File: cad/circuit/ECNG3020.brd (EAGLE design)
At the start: 100 x 61 mm, 30 parts, among them Q1 16Mhz, T1 2N3904, T2 2N3904, T3 2N3904, T4 2N3904, T5 2N3904, U1 ATMEGA328P-PU, X1 22-23-2021, X2 22-23-2021, X3 22-23-2021, X4 22-23-2021, X5 22-23-2021, X6 22-23-2021, X7 22-23-2021

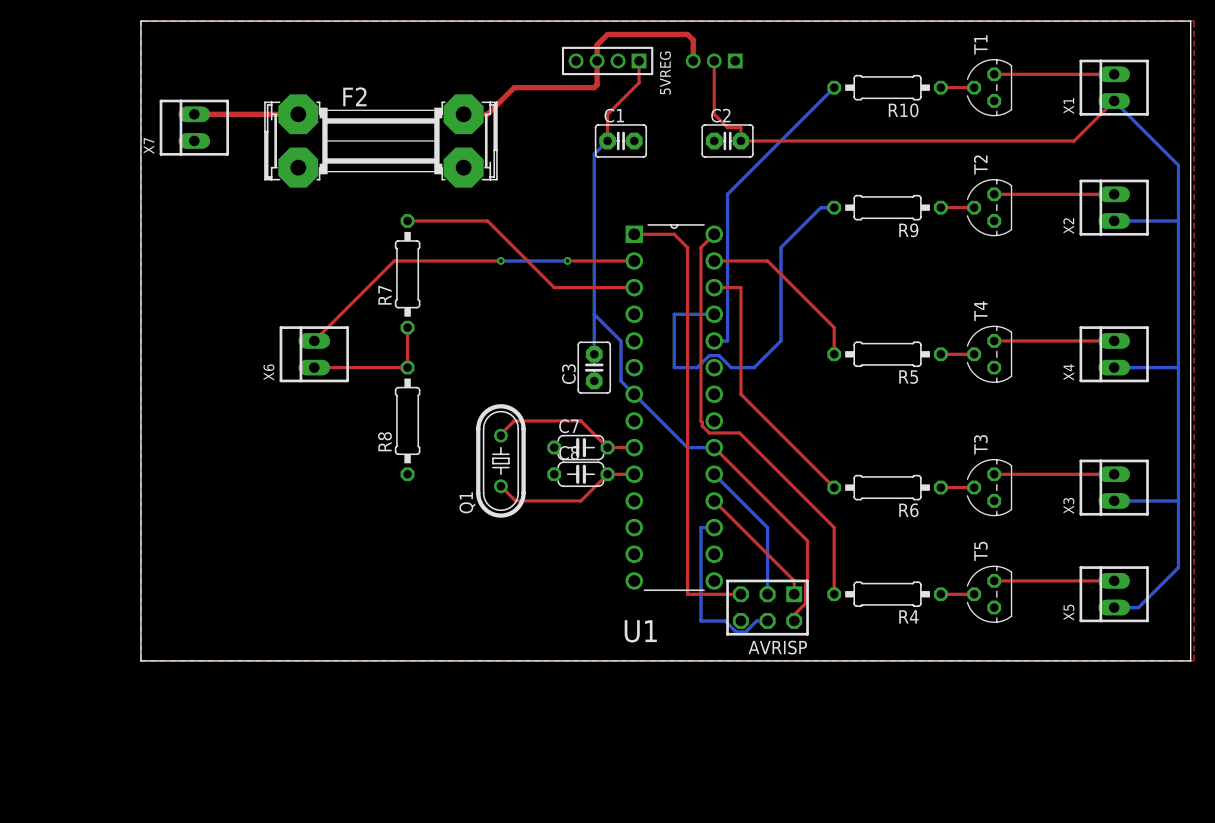
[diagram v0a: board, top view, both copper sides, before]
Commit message: Updated the PCB to use I2C instead of UART
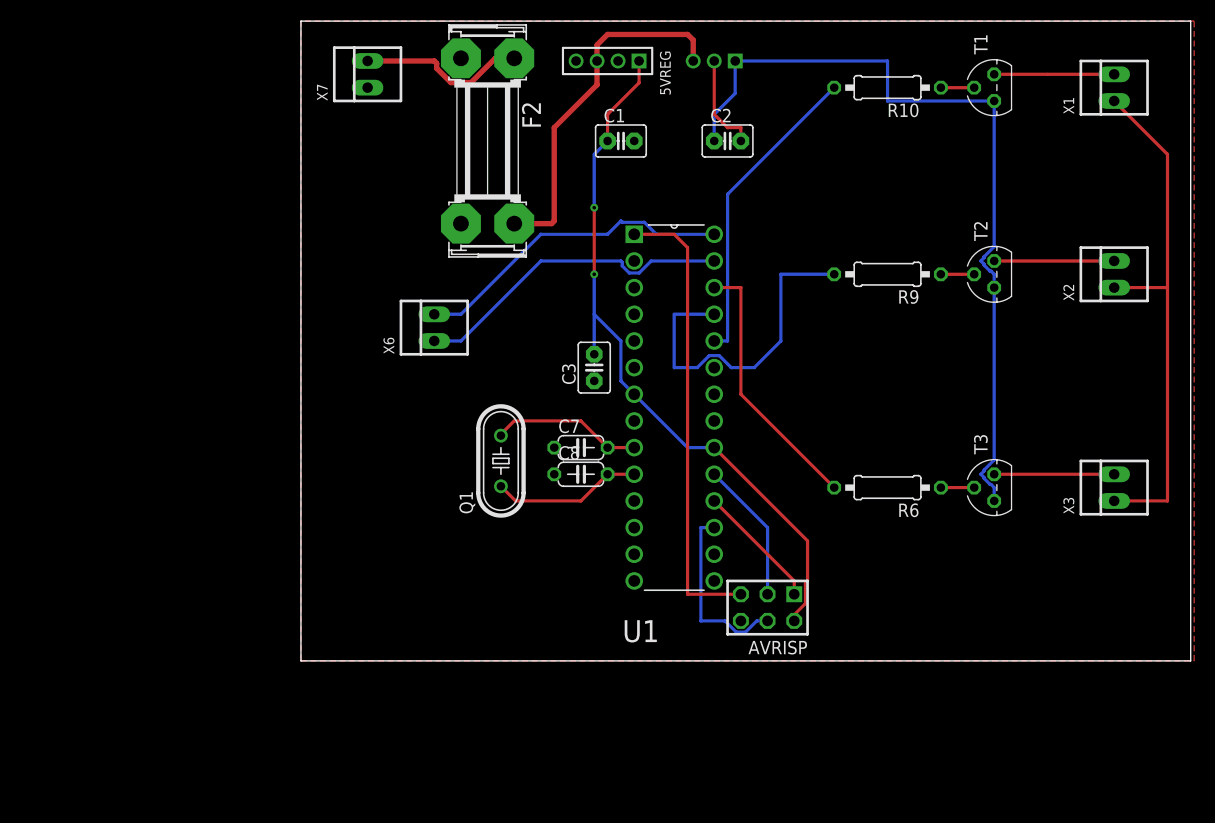
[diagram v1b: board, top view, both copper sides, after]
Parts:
- removed R4, R5, R8: 10k, rcl:0207/10
- removed R7: 5k1, rcl:0207/10
- removed T4, T5: 2N3904, transistor-neu-to92:TO92
- removed X4, X5: 22-23-2021, con-molex:22-23-2021
- moved X7 17.3 mm to (33.0, 68.6)
- moved X6 11.7 mm to (39.4, 44.5)
- moved F2 10.2 mm to (44.5, 62.2), turned to 270 degrees
- moved R9 6.35 mm to (82.5, 49.5)
- moved T2 6.35 mm to (92.7, 49.5)
- moved X2 6.35 mm to (104.1, 49.5)
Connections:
- removed net N$16: R5.1, T4.2
- removed net N$17: R5.2, U1.27
- removed net N$18: R4.2, U1.28
- removed net N$8: T5.1, X5.2
- removed net N$9: T4.1, X4.2
- removed net RX: R7.1, R8.2, X6.1
- new net SCL: U1.28, X6.2
- new net SDA: U1.27, X6.1
- net 3.3: no longer X1.1, X2.1, X3.1, X4.1, X5.1
- net GND: no longer R8.1, T4.3, T5.3
- net N$7: now also X1.1, X2.1, X3.1; no longer R4.1, T5.2
- net RXM: no longer X6.2
- net TXM: no longer R7.2
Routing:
- net 3.3: track 119.6 -> 9.42 mm
- net GND: track 0.00 -> 77.2 mm
- net N$7: track 3.18 -> 50.4 mm
- net N$18: track 41.8 -> 0.00 mm
- net RXM: track 33.6 -> 0.00 mm, vias 2 -> 0
- net SDA: track 0.00 -> 31.0 mm
- net SCL: track 0.00 -> 30.9 mm
- net TXM: track 24.2 -> 0.00 mm
- net N$17: track 16.6 -> 0.00 mm
- net RX: track 12.7 -> 0.00 mm
- net N$9: track 11.4 -> 0.00 mm
- net N$8: track 11.4 -> 0.00 mm
- net N$13: track 9.91 -> 16.1 mm
- net 12V: track 29.5 -> 34.2 mm
- net N$2: track 36.6 -> 32.5 mm
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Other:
- board size 100 x 61 mm -> 84.8 x 61 mm

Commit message: Updated the schematic and board
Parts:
- moved R10 50.7 mm to (63.5, 20.3)
- moved T1 50.2 mm to (74.9, 20.3)
- moved X1 49.4 mm to (88.9, 20.3)
- moved X7 45.1 mm to (8.89, 30.5)
- moved F2 38.9 mm to (20.3, 31.8), turned to 90 degrees
- moved C8 33.2 mm to (30.5, 6.35), turned to 180 degrees
- moved Q1 33.2 mm to (21.6, 8.89)
- moved C7 31.4 mm to (30.5, 11.4), turned to 180 degrees
- moved X6 31.1 mm to (69.8, 50.8)
- moved R9 27.9 mm to (63.5, 29.2), flipped to the bottom, turned to 0 degrees
- moved T2 27.0 mm to (74.9, 29.2)
- moved C1 25.7 mm to (35.6, 48.3)
- moved X2 25.4 mm to (88.9, 29.2)
- moved C3 25.0 mm to (30.5, 34.3)
- moved C2 23.6 mm to (48.3, 48.3)
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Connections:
- removed net RXM: U1.2
- removed net TXM: U1.3
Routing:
- net GND: track 77.2 -> 0.00 mm
- net N$7: track 50.4 -> 27.7 mm
- net N$2: track 32.5 -> 12.5 mm
- net N$4: track 25.3 -> 13.8 mm
- net 12V: track 34.2 -> 45.1 mm
- net N$1: track 29.6 -> 18.8 mm
- net N$5: track 14.3 -> 25.0 mm
- net VCC: track 69.3 -> 60.6 mm, vias 2 -> 0
- net N$3: track 14.4 -> 21.0 mm
- net MOSI: track 17.4 -> 12.8 mm
- net RST: track 43.7 -> 47.3 mm
- net SDA: track 31.0 -> 28.1 mm
- net SCL: track 30.9 -> 28.1 mm
- net N$12: track 11.4 -> 14.0 mm
- net N$11: track 11.4 -> 14.0 mm
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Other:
- board size 84.8 x 61 mm -> 96.5 x 65.7 mm

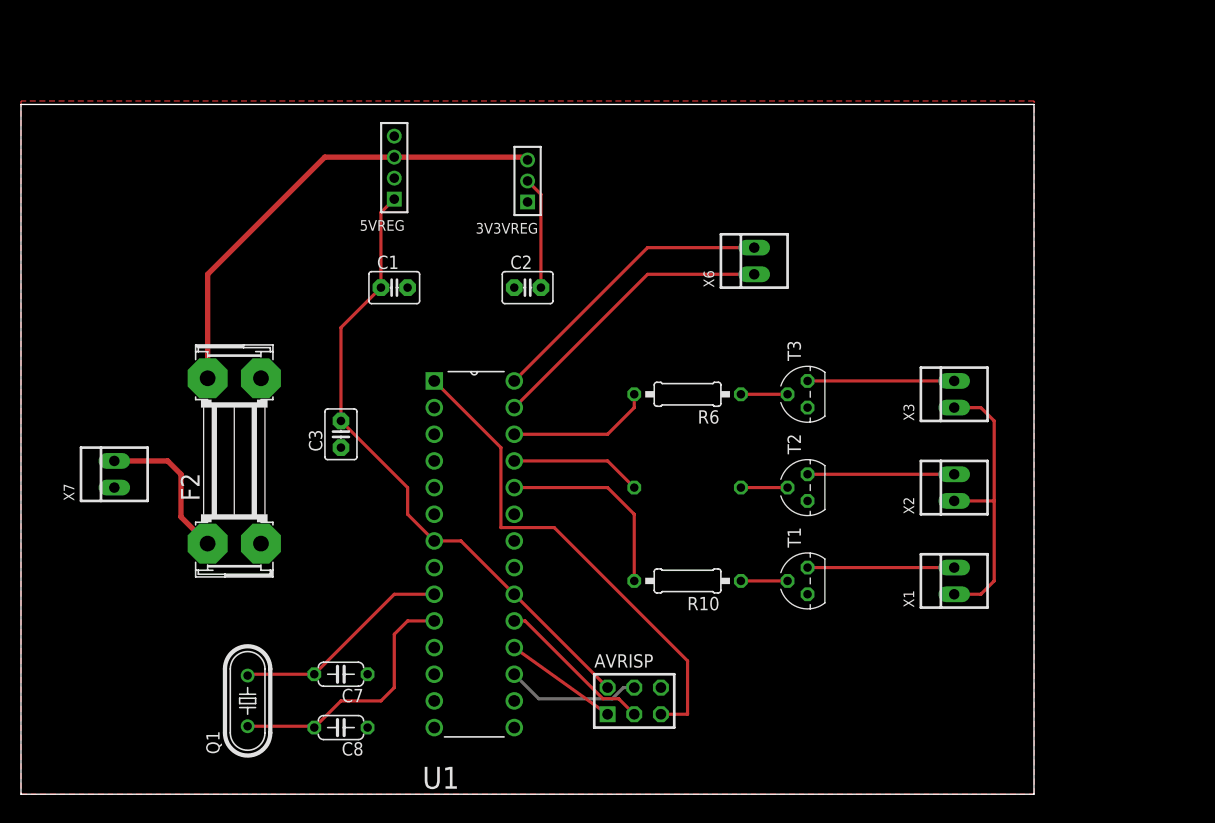
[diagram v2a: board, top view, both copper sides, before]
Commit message: Added in rpi power source
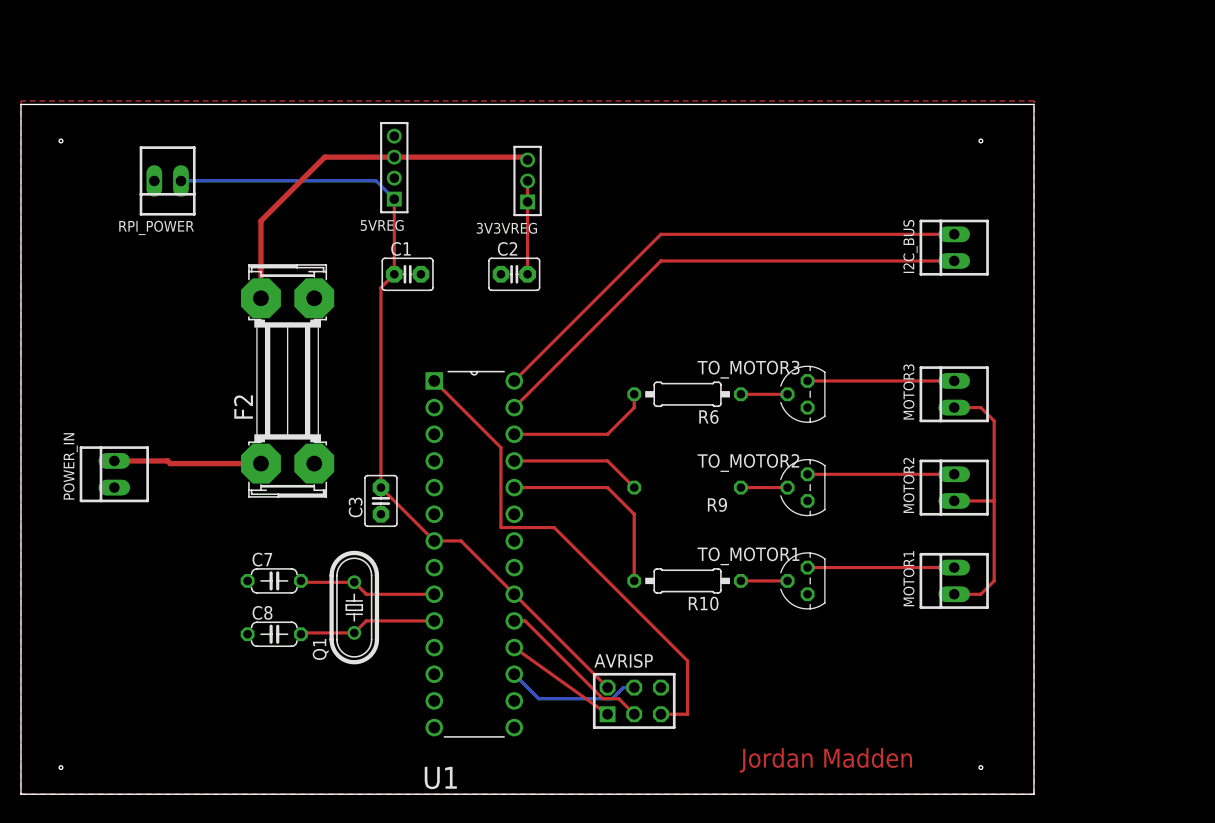
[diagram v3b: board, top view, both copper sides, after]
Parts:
- removed X6: 22-23-2021, con-molex:22-23-2021
- added I2C_BUS, RPI_POWER: 22-23-2021, con-molex:22-23-2021
- moved Q1 13.5 mm to (31.8, 17.8)
- moved C7 10.9 mm to (24.1, 20.3), turned to 0 degrees
- moved C8 10.9 mm to (24.1, 15.2), turned to 0 degrees
- moved F2 9.16 mm to (25.4, 39.4)
- moved C3 7.41 mm to (34.3, 27.9)
- moved C1 1.80 mm to (36.8, 49.5)
- moved C2 1.80 mm to (47.0, 49.5)
- renumbered T1 to TO_MOTOR1, T2 to TO_MOTOR2, T3 to TO_MOTOR3, X1 to MOTOR1, X2 to MOTOR2, X3 to MOTOR3, X7 to POWER_IN
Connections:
- net GND: now also RPI_POWER.2
- net SCL: now also I2C_BUS.2; no longer X6.2
- net SDA: now also I2C_BUS.1; no longer X6.1
- net VCC: now also RPI_POWER.1
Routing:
- net SDA: track 28.1 -> 47.7 mm
- net SCL: track 28.1 -> 47.7 mm
- net VCC: track 60.6 -> 78.5 mm
- net N$5: track 25.0 -> 13.2 mm
- net 12V: track 45.1 -> 35.4 mm
- net N$3: track 21.0 -> 13.2 mm
- net 3.3: track 10.7 -> 8.89 mm
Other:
- board text added: "Jordan Madden"

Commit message: Made pcb smaller and added larger holes
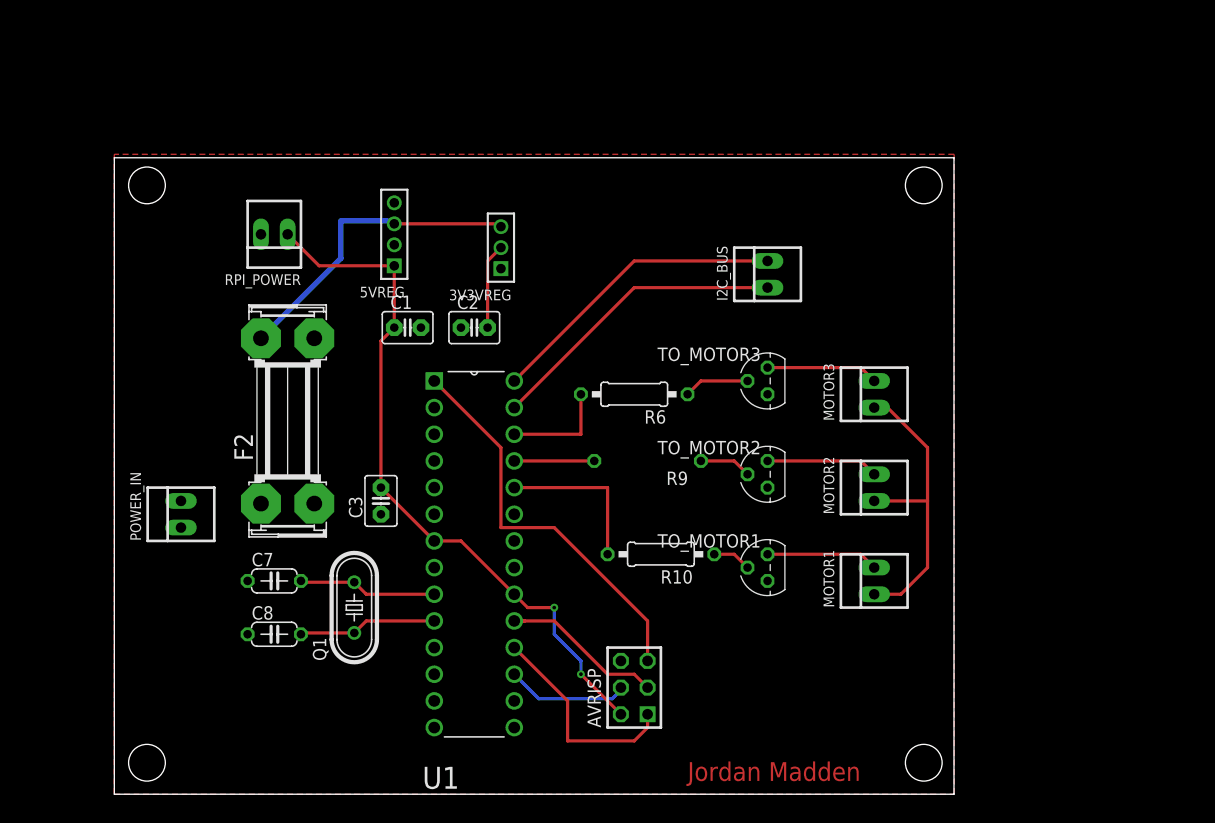
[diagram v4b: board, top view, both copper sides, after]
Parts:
- moved I2C_BUS 18.0 mm to (71.1, 49.5)
- moved RPI_POWER 11.4 mm to (24.1, 53.3)
- moved MOTOR1 7.62 mm to (81.3, 20.3)
- moved MOTOR2 7.62 mm to (81.3, 29.2)
- moved MOTOR3 7.62 mm to (81.3, 38.1)
- moved POWER_IN 7.41 mm to (15.2, 26.7)
- moved 3V3VREG 6.84 mm to (45.7, 52.1)
- moved C2 6.35 mm to (43.2, 44.5)
- moved 5VREG 6.35 mm to (35.6, 53.3)
- moved C1 5.08 mm to (36.8, 44.5)
- moved R6 5.08 mm to (58.4, 38.1)
- moved R9 4.58 mm to (59.7, 31.8)
- moved TO_MOTOR1 4.02 mm to (71.1, 21.6)
- moved TO_MOTOR2 4.02 mm to (71.1, 30.5)
- moved TO_MOTOR3 4.02 mm to (71.1, 39.4)
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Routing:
- net SDA: track 47.7 -> 28.9 mm
- net SCL: track 47.7 -> 28.9 mm
- net N$13: track 14.1 -> 0.00 mm
- net VCC: track 78.5 -> 67.1 mm, vias 0 -> 2
- net MISO: track 10.9 -> 20.4 mm
- net RST: track 47.3 -> 38.1 mm
- net 12V: track 35.4 -> 29.8 mm
- net N$2: track 12.5 -> 7.62 mm
- net N$4: track 13.8 -> 10.2 mm
- net N$1: track 18.8 -> 15.2 mm
- net N$12: track 14.0 -> 10.7 mm
- net N$11: track 14.0 -> 10.7 mm
- net N$10: track 14.0 -> 10.7 mm
- net N$15: track 4.45 -> 6.24 mm
- net N$7: track 27.7 -> 29.3 mm
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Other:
- board size 96.5 x 65.7 mm -> 80 x 60.6 mm
